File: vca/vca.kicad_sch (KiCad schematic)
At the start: 22 parts, among them U4 STM32F103C6Tx, Y1 Crystal_8Mhz

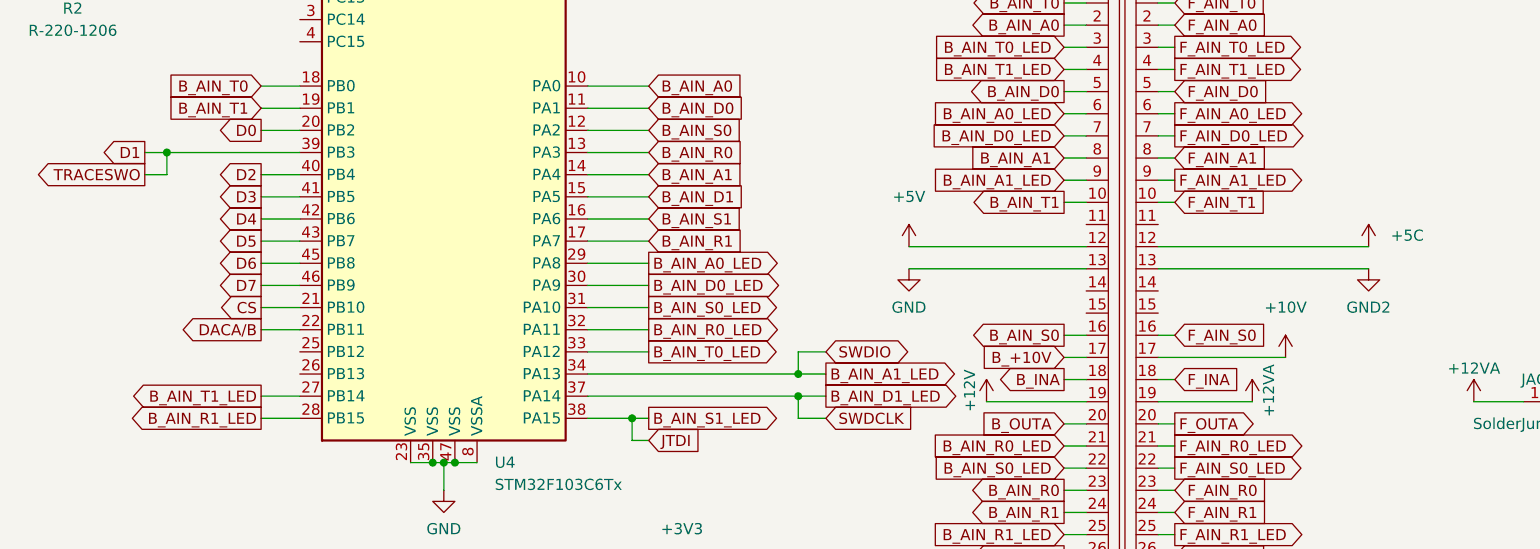
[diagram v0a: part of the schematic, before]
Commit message: Added buttons, refactored front panel, refactored power part, wip
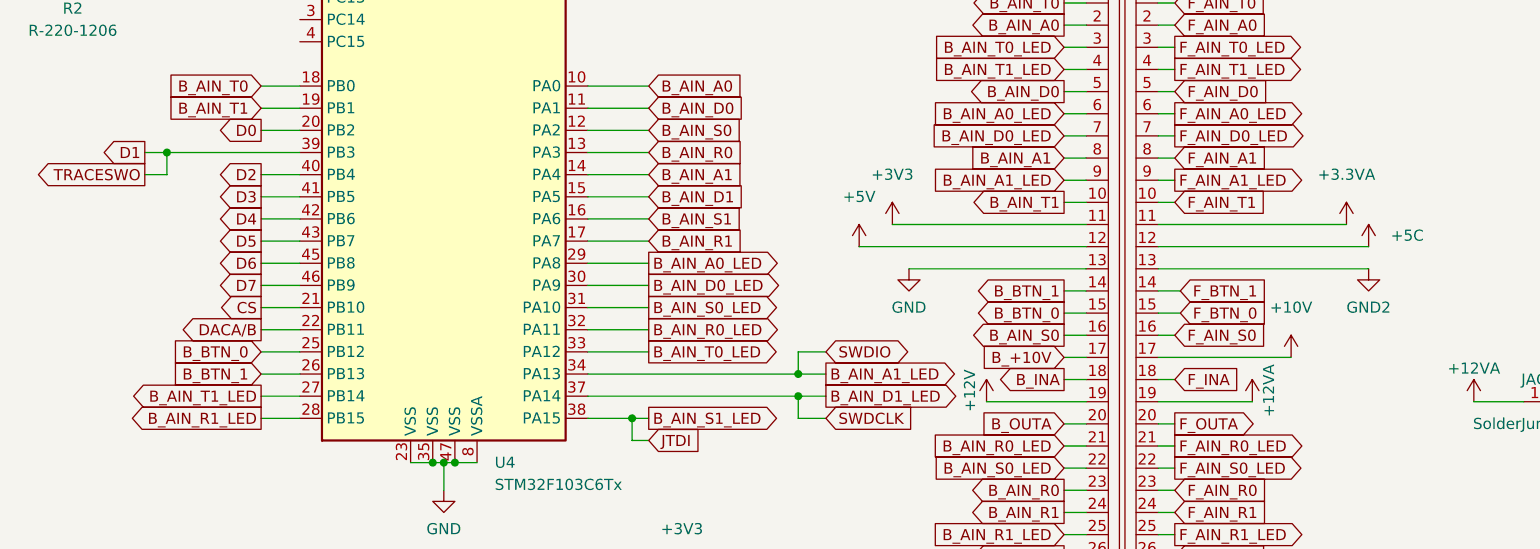
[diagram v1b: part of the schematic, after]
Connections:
- net +3V3: now also CON_BACK1.11
- net B_BTN_1: now reaches CON_BACK1.14
- net B_BTN_1: now also U4.26 (PB13)
- net B_BTN_0: now reaches CON_BACK1.15
- net B_BTN_0: now also U4.25 (PB12)
- net +3.3VA: now reaches CON_FRONT1.11
- net F_BTN_1: now reaches CON_FRONT1.14
- net F_BTN_0: now reaches CON_FRONT1.15

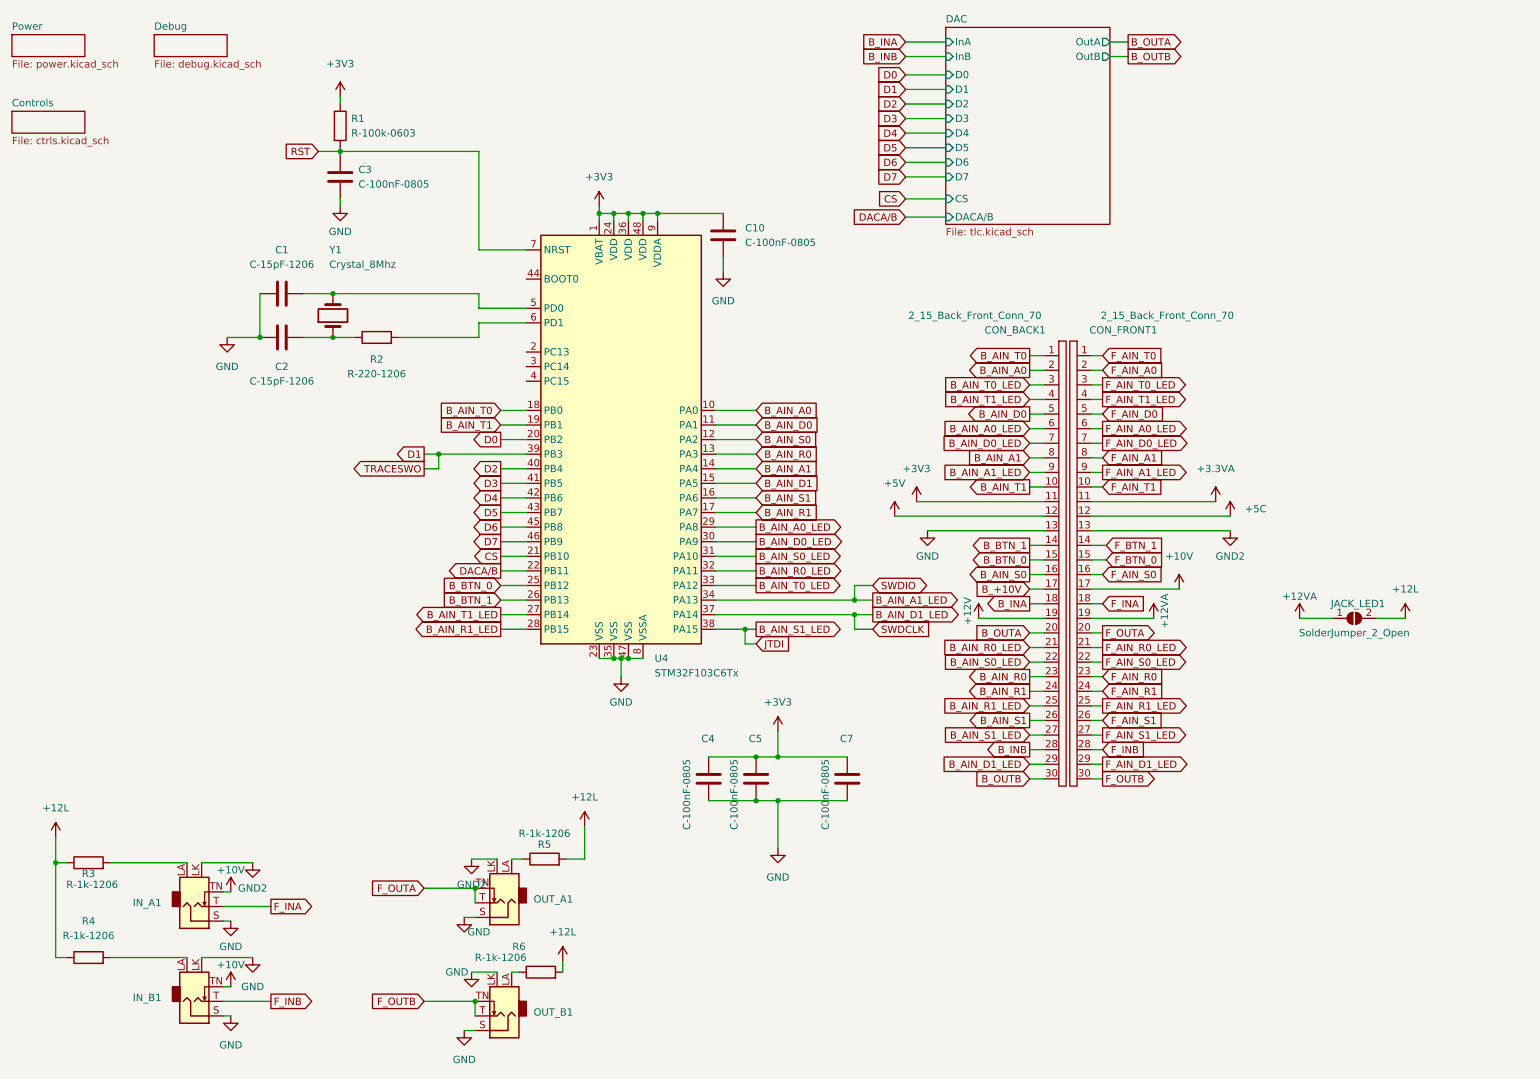
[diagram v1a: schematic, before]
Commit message: fixing drc issues
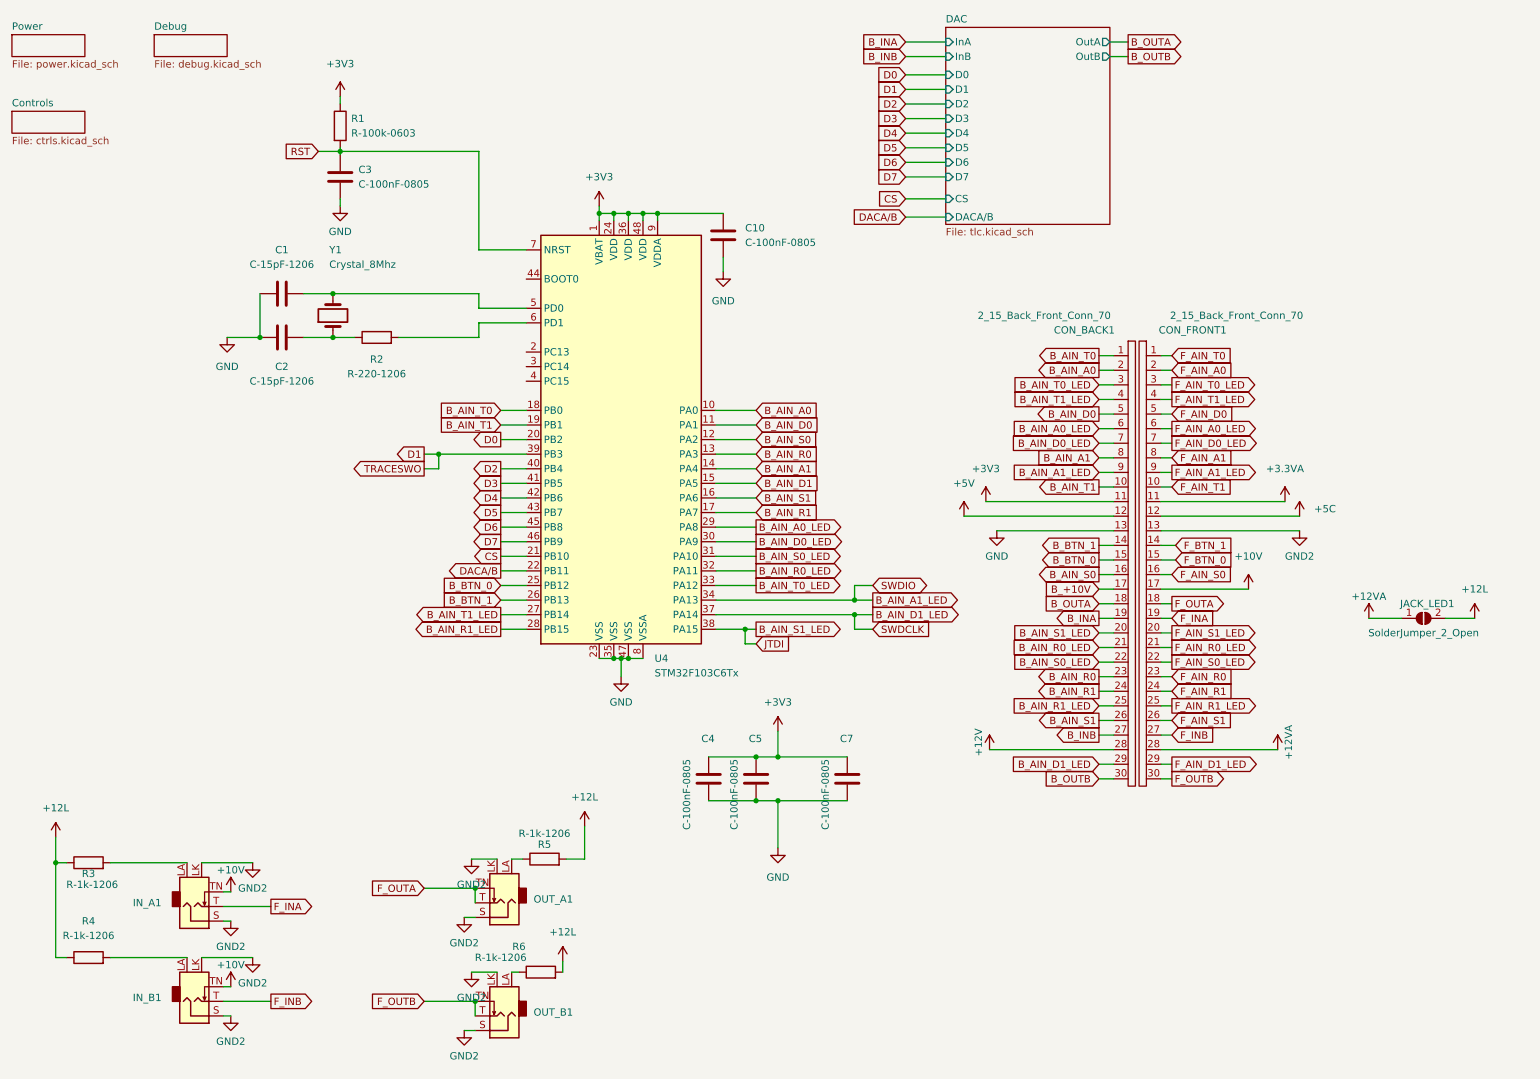
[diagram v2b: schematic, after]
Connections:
- net +12V: now also CON_BACK1.28; no longer CON_BACK1.19
- net +12VA: now also CON_FRONT1.28; no longer CON_FRONT1.19
- net B_AIN_S1_LED: now also CON_BACK1.20; no longer CON_BACK1.27
- net B_INA: now also CON_BACK1.19; no longer CON_BACK1.18
- net B_INB: now also CON_BACK1.27; no longer CON_BACK1.28
- net B_OUTA: now also CON_BACK1.18; no longer CON_BACK1.20
- net F_AIN_S1_LED: now also CON_FRONT1.20; no longer CON_FRONT1.27
- net F_INA: now also CON_FRONT1.19; no longer CON_FRONT1.18
- net F_INB: now also CON_FRONT1.27; no longer CON_FRONT1.28
- net F_OUTA: now also CON_FRONT1.18; no longer CON_FRONT1.20
- net GND: no longer IN_A1.S, IN_B1.LK, IN_B1.S, OUT_A1.S, OUT_B1.LK, OUT_B1.S
- net GND2: now also IN_A1.S, IN_B1.LK, IN_B1.S, OUT_A1.S, OUT_B1.LK, OUT_B1.S
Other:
- moved on the sheet: CON_BACK1, CON_FRONT1, JACK_LED1

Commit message: DRC Free first version
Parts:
- added L1: VikingCube_Logo, eurorack:logo_small, symbol eurorack:VikingCube_Logo
- added L2: VikingCube_Logo, eurorack:logo_small_txt, symbol eurorack:VikingCube_Logo
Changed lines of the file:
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@@
     (pin "2")
+  )
+  (symbol (lib_id "eurorack:VikingCube_Logo") (at 246.38 17.145 0) (unit 1)
+    (in_bom no) (on_board yes) (fields_autoplaced)
+    (property "Reference" "L1" (id 0) (at 247.015 15.8749 0)
+      (effects (font (size 1.27 1.27)) (justify left))
+    )
+    (property "Value" "VikingCube_Logo" (id 1) (at 247.015 18.4149 0)
+      (effects (font (size 1.27 1.27)) (justify left))
+    )
+    (property "Footprint" "eurorack:logo_small" (id 2) (at 246.38 17.145 0)
+      (effects (font (size 1.27 1.27)) hide)
+    )
+    (property "Datasheet" "" (id 3) (at 246.38 17.145 0)
+      (effects (font (size 1.27 1.27)) hide)
+    )
   )
   (symbol (lib_id "power:GND2") (at 57.15 162.56 0) (unit 1)
@@
     )
     (pin "1")
+  )
+  (symbol (lib_id "Graphic:Logo_Open_Hardware_Small") (at 273.685 22.225 0) (unit 1)
+    (in_bom yes) (on_board yes) (fields_autoplaced)
+    (property "Reference" "#LOGO1" (id 0) (at 273.685 15.24 0)
+      (effects (font (size 1.27 1.27)) hide)
+    )
+    (property "Value" "Logo_Open_Hardware_Small" (id 1) (at 273.685 27.94 0)
+      (effects (font (size 1.27 1.27)) hide)
+    )
+    (property "Footprint" "" (id 2) (at 273.685 22.225 0)
+      (effects (font (size 1.27 1.27)) hide)
+    )
+    (property "Datasheet" "~" (id 3) (at 273.685 22.225 0)
+      (effects (font (size 1.27 1.27)) hide)
+    )
   )
   (symbol (lib_id "power:GND2") (at 93.98 172.085 0) (unit 1)
@@
     )
     (pin "1")
+  )
+  (symbol (lib_id "eurorack:VikingCube_Logo") (at 245.745 22.86 0) (unit 1)
+    (in_bom no) (on_board yes) (fields_autoplaced)
+    (property "Reference" "L2" (id 0) (at 246.38 21.5899 0)
+      (effects (font (size 1.27 1.27)) (justify left))
+    )
+    (property "Value" "VikingCube_Logo" (id 1) (at 246.38 24.1299 0)
+      (effects (font (size 1.27 1.27)) (justify left))
+    )
+    (property "Footprint" "eurorack:logo_small_txt" (id 2) (at 245.745 22.86 0)
+      (effects (font (size 1.27 1.27)) hide)
+    )
+    (property "Datasheet" "" (id 3) (at 245.745 22.86 0)
+      (effects (font (size 1.27 1.27)) hide)
+    )
   )
   (symbol (lib_id "power:GND") (at 148.59 160.02 0) (unit 1)
@@
   )
   (symbol_instances
+    (path "/48c90ceb-fe4b-459d-99b0-3cec0ac261c8"
+      (reference "#LOGO1") (unit 1) (value "Logo_Open_Hardware_Small") (footprint "")
+    )
     (path "/91f87fc6-c431-4dbd-bf9a-22d85a993784/aa7c0a7c-9074-484b-9343-5acf98c9bf0a"
       (reference "#PWR015") (unit 1) (value "GND") (footprint "")
@@
       (reference "JP2") (unit 1) (value "Jumper_2_Open") (footprint "Jumper:SolderJumper-2_P1.3mm_Open_Pad1.0x1.5mm")
     )
+    (path "/0a00820f-b009-4337-9c46-d197f9b931bc"
+      (reference "L1") (unit 1) (value "VikingCube_Logo") (footprint "eurorack:logo_small")
+    )
+    (path "/7361d402-43a4-428d-b00e-fa83637659d5"
+      (reference "L2") (unit 1) (value "VikingCube_Logo") (footprint "eurorack:logo_small_txt")
+    )
     (path "/a80cea03-1367-4c37-b52b-f2a6e0348e8a"

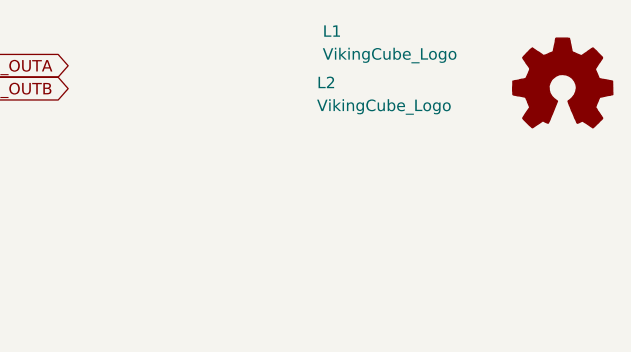
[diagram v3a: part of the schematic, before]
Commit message: working on the cover panel
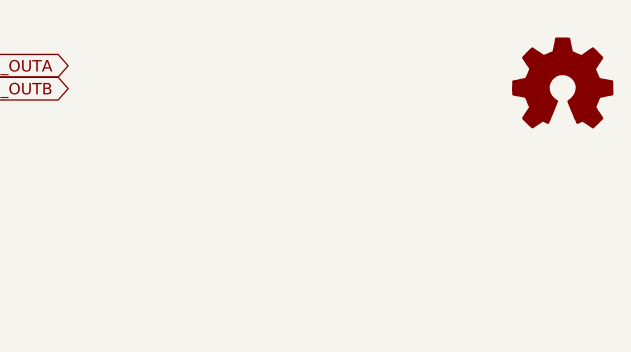
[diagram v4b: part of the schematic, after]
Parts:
- removed L1: VikingCube_Logo, eurorack:logo_small, symbol eurorack:VikingCube_Logo
- removed L2: VikingCube_Logo, eurorack:logo_small_txt, symbol eurorack:VikingCube_Logo
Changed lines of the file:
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@@
     (pin "2")
-  )
-  (symbol (lib_id "eurorack:VikingCube_Logo") (at 246.38 17.145 0) (unit 1)
-    (in_bom no) (on_board yes) (fields_autoplaced)
-    (property "Reference" "L1" (id 0) (at 247.015 15.8749 0)
-      (effects (font (size 1.27 1.27)) (justify left))
-    )
-    (property "Value" "VikingCube_Logo" (id 1) (at 247.015 18.4149 0)
-      (effects (font (size 1.27 1.27)) (justify left))
-    )
-    (property "Footprint" "eurorack:logo_small" (id 2) (at 246.38 17.145 0)
-      (effects (font (size 1.27 1.27)) hide)
-    )
-    (property "Datasheet" "" (id 3) (at 246.38 17.145 0)
-      (effects (font (size 1.27 1.27)) hide)
-    )
   )
   (symbol (lib_id "power:GND2") (at 57.15 162.56 0) (unit 1)
@@
     )
     (pin "1")
-  )
-  (symbol (lib_id "eurorack:VikingCube_Logo") (at 245.745 22.86 0) (unit 1)
-    (in_bom no) (on_board yes) (fields_autoplaced)
-    (property "Reference" "L2" (id 0) (at 246.38 21.5899 0)
-      (effects (font (size 1.27 1.27)) (justify left))
-    )
-    (property "Value" "VikingCube_Logo" (id 1) (at 246.38 24.1299 0)
-      (effects (font (size 1.27 1.27)) (justify left))
-    )
-    (property "Footprint" "eurorack:logo_small_txt" (id 2) (at 245.745 22.86 0)
-      (effects (font (size 1.27 1.27)) hide)
-    )
-    (property "Datasheet" "" (id 3) (at 245.745 22.86 0)
-      (effects (font (size 1.27 1.27)) hide)
-    )
   )
   (symbol (lib_id "power:GND") (at 148.59 160.02 0) (unit 1)
@@
       (reference "JP2") (unit 1) (value "Jumper_2_Open") (footprint "Jumper:SolderJumper-2_P1.3mm_Open_Pad1.0x1.5mm")
     )
-    (path "/0a00820f-b009-4337-9c46-d197f9b931bc"
-      (reference "L1") (unit 1) (value "VikingCube_Logo") (footprint "eurorack:logo_small")
-    )
-    (path "/7361d402-43a4-428d-b00e-fa83637659d5"
-      (reference "L2") (unit 1) (value "VikingCube_Logo") (footprint "eurorack:logo_small_txt")
-    )
     (path "/a80cea03-1367-4c37-b52b-f2a6e0348e8a"
